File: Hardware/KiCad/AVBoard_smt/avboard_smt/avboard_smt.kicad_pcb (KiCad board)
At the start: 4 copper layers, 177 x 152.1 mm, 119 parts, among them IC1 AS7C256A-10TIN, IC2_AUD0 7432N, IC36 4040N, IC37 7430N, IC39 7400N, IC40 4040N, IC41 7400N, IC43 7400N, IC44 7486N, IC45 7400N, IC46 74257N, IC47 74257N, IC48 74564N, IC4_AUD0 7400N, IC53 7404N, IC6_AUD0 7474N, IC7_AUD0 LM358N, IC9 AS7C256A-10TIN, J1 5V, J2 VID_TO_MOBO, U1 W65C02SP, U2 THS7374, U3 74AHC373, U4 74AHC373, U5 74AHC373, U6 74AC00, U7 74VHC74, U8 74HC244, U9 74HC244

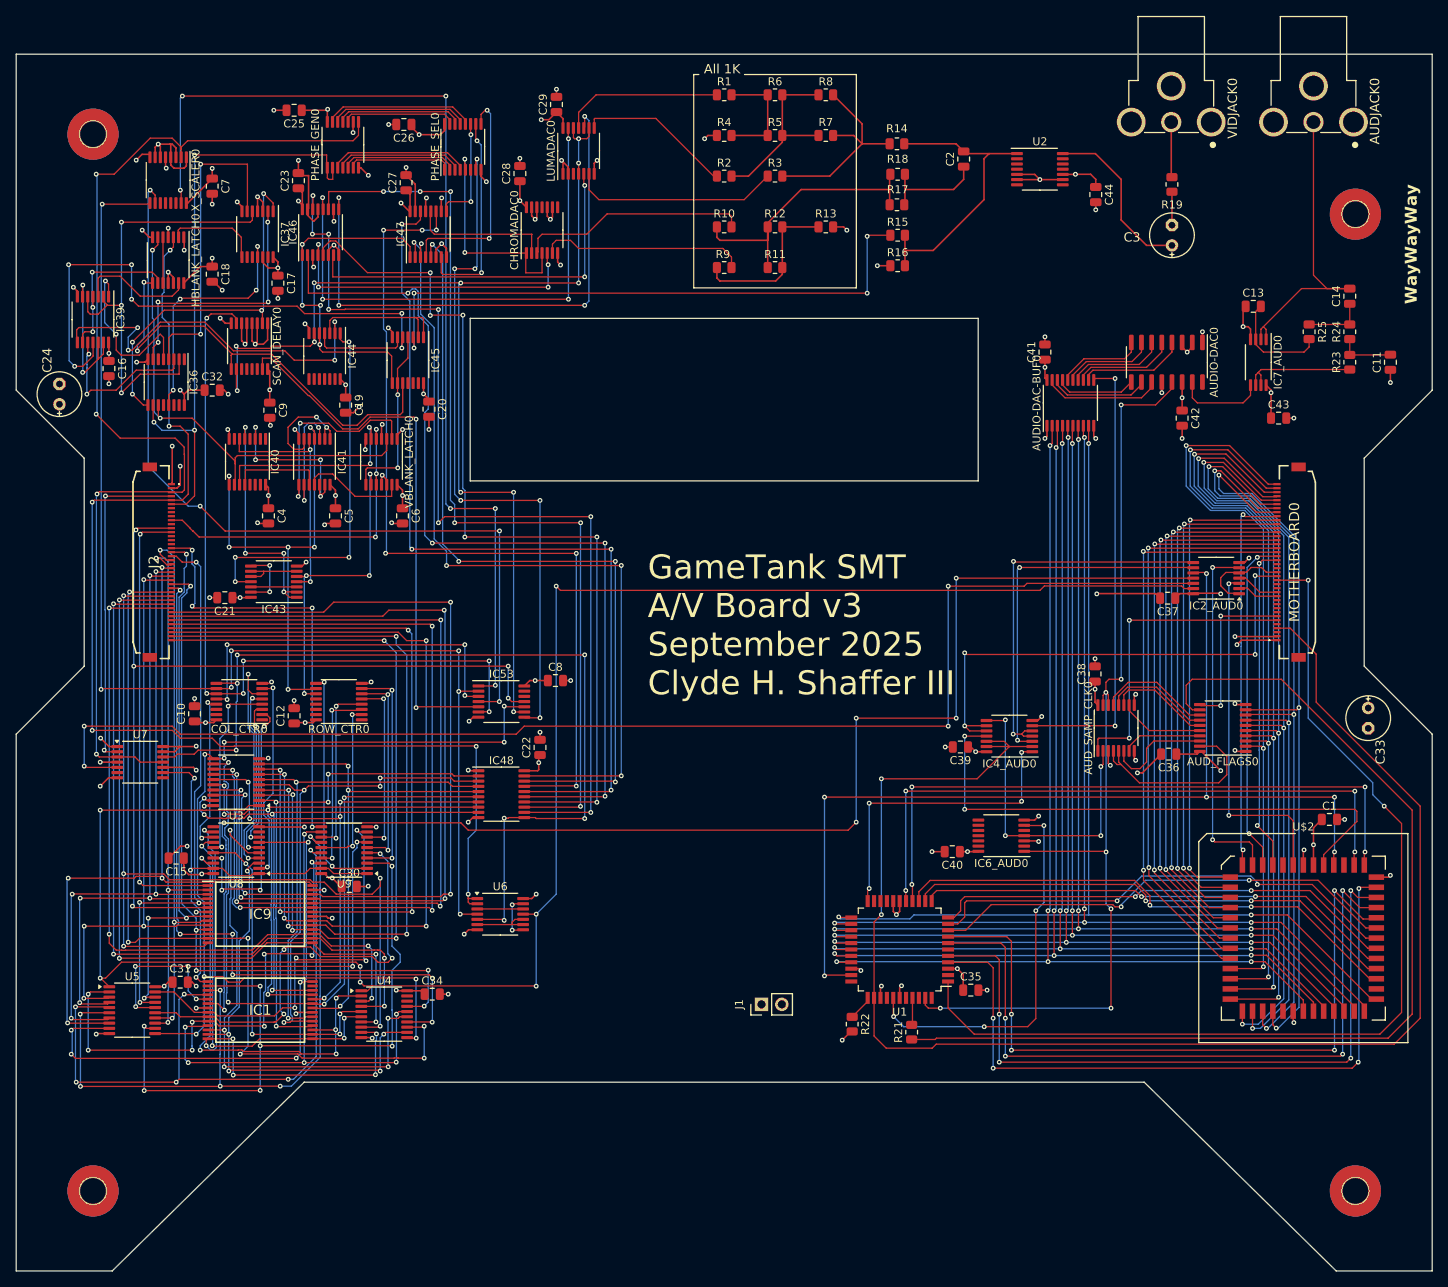
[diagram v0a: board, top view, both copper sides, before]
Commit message: design out the 4K dualport ram
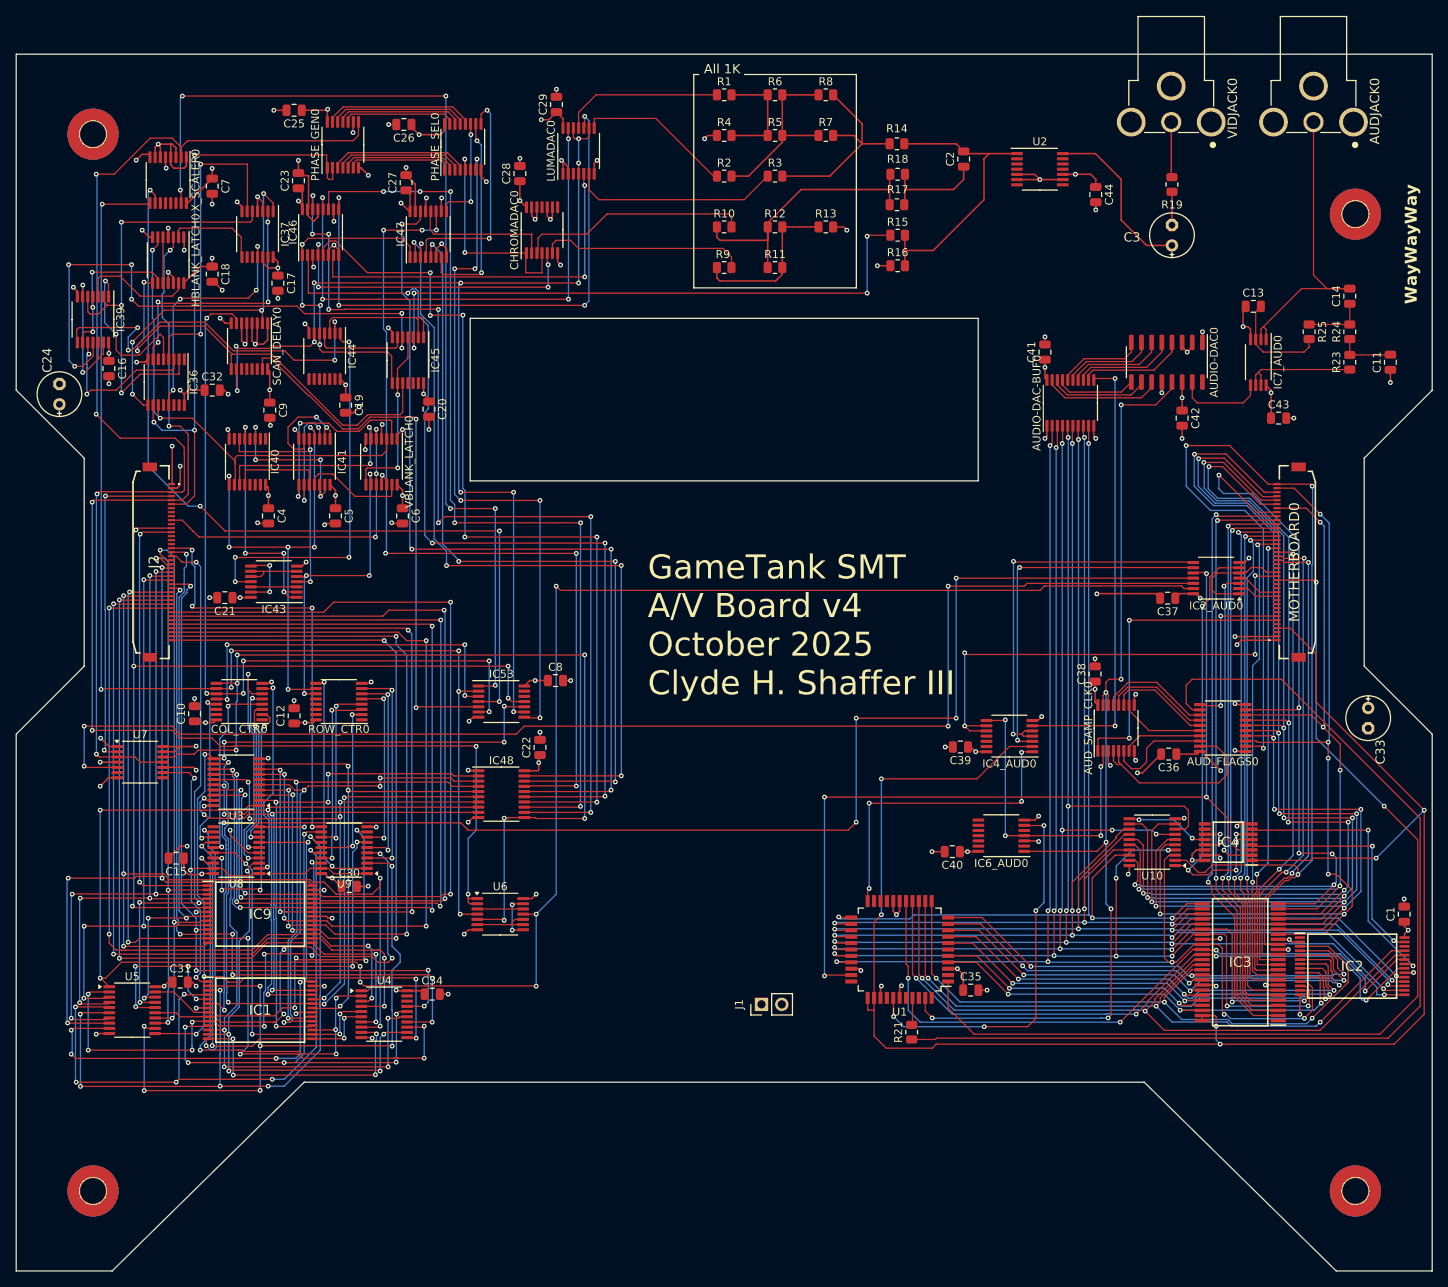
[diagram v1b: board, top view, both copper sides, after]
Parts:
- removed R22: 3.3k, Resistor_SMD:R_0805_2012Metric
- removed U$2: PDPRAM_4KPLCC52S, Package_LCC:PLCC-52_SMD-Socket
- added IC2: IS61C64AL-10TLI, SamacSys_Parts:SOP55P1340X120-28N, F.Cu at (227.0, 155.5)
- added IC3: SN74CBT16210CDLR, SamacSys_Parts:SOP64P1035X279-48N, F.Cu at (213.0, 155.0)
- added IC4: 74VHC157FT, SamacSys_Parts:SOP65P640X120-16N, F.Cu at (211.5, 140.0)
- added U10: 74AHC373, Package_SO:TSSOP-20_4.4x6.5mm_P0.65mm, F.Cu at (202.0, 140.0)
- moved C1 15.1 mm to (233.5, 149.0), turned to 90 degrees
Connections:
- IC2_AUD0 pad 3: Net-(IC2_AUD0A-O) -> /signals_4/Sys_ARAM_~{WE}
- IC2_AUD0 pad 6: Net-(IC2_AUD0B-O) -> /signals_4/Sys_ARAM_~{OE}
- IC4_AUD0 pad 11: Net-(IC4_AUD0D-O) -> unconnected-(IC4_AUD0D-O-Pad11)
- IC4_AUD0 pad 12: /signals_4/CLK14_AUD -> unconnected-(IC4_AUD0D-I0-Pad12)
- IC4_AUD0 pad 13: /signals_4/CLK14_AUD -> unconnected-(IC4_AUD0D-I1-Pad13)
- U1 pad 36: Net-(U1-BE) -> /signals_4/CLK14_AUD
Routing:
- net Net-(IC4_AUD0D-O): track 69.4 -> 0.00 mm, vias 2 -> 0
- net /signals_4/Sys_ARAM_~{OE}: track 0.00 -> 55.8 mm, vias 0 -> 4
- net Net-(AUD_FLAGS0A-1D): track 91.6 -> 143.9 mm, vias 3 -> 4
- net Net-(IC2_AUD0B-O): track 44.6 -> 0.00 mm, vias 2 -> 0
- net Net-(IC2_AUD0A-O): track 44.2 -> 0.00 mm, vias 2 -> 0
- net Net-(AUD_FLAGS0A-3D): track 94.6 -> 133.8 mm, vias 3 -> 6
- net /signals_4/Sys_ARAM_~{WE}: track 0.00 -> 38.9 mm, vias 0 -> 2
- net Net-(AUD_FLAGS0A-4D): track 96.0 -> 134.0 mm, vias 3 -> 6
- net /signals_4/ARAM_~{OE}: track 0.00 -> 35.1 mm, vias 0 -> 2
- net Net-(AUD_FLAGS0A-5D): track 97.7 -> 131.0 mm, vias 3 -> 6
- net /signals_4/AD3: track 132.6 -> 165.2 mm, vias 5 -> 7
- net /signals_4/AA0: track 88.4 -> 58.0 mm, vias 4 -> 3
- net /signals_4/ARAM_~{WE}: track 0.00 -> 29.5 mm, vias 0 -> 2
- net /signals_4/AA2: track 88.8 -> 59.9 mm, vias 4 -> 3
- net Net-(AUD_FLAGS0A-6D): track 97.4 -> 126.2 mm, vias 3 -> 6
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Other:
- board text added: "GameTank SMT A/V Board v4 October 2025 Clyde H. Shaffer III"
- board text removed: "GameTank SMT A/V Board v3 September 2025 Clyde H. Shaffer III"

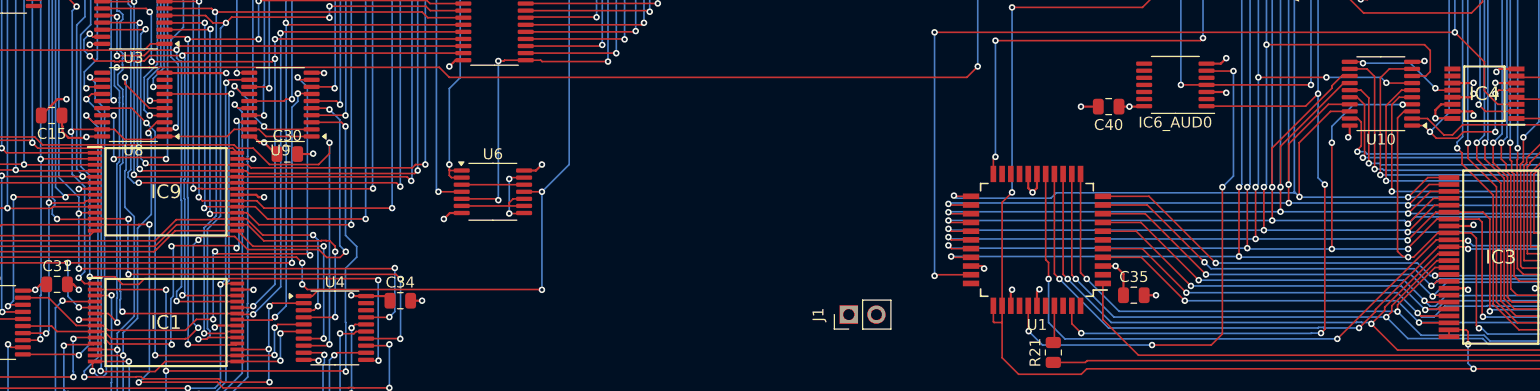
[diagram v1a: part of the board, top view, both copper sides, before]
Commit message: connect loose unused inputs to ground
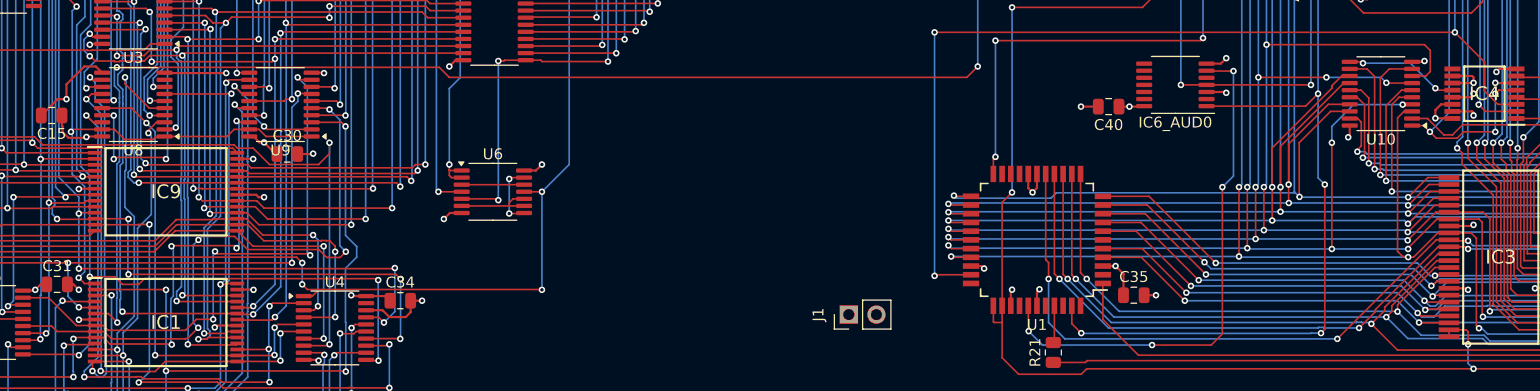
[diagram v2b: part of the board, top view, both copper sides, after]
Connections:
- IC4 pad 10: /signals_4/ACP_ARAM_~{CE} -> GND
- IC4 pad 9: /signals_4/ARAM_~{CE} -> unconnected-(IC4-3Y-Pad9)
- U4 pad 18: unconnected-(U4-D7-Pad18) -> GND
- U8 pad 11: unconnected-(U8-2A3-Pad11) -> GND
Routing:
- net GND: track 234.5 -> 248.1 mm

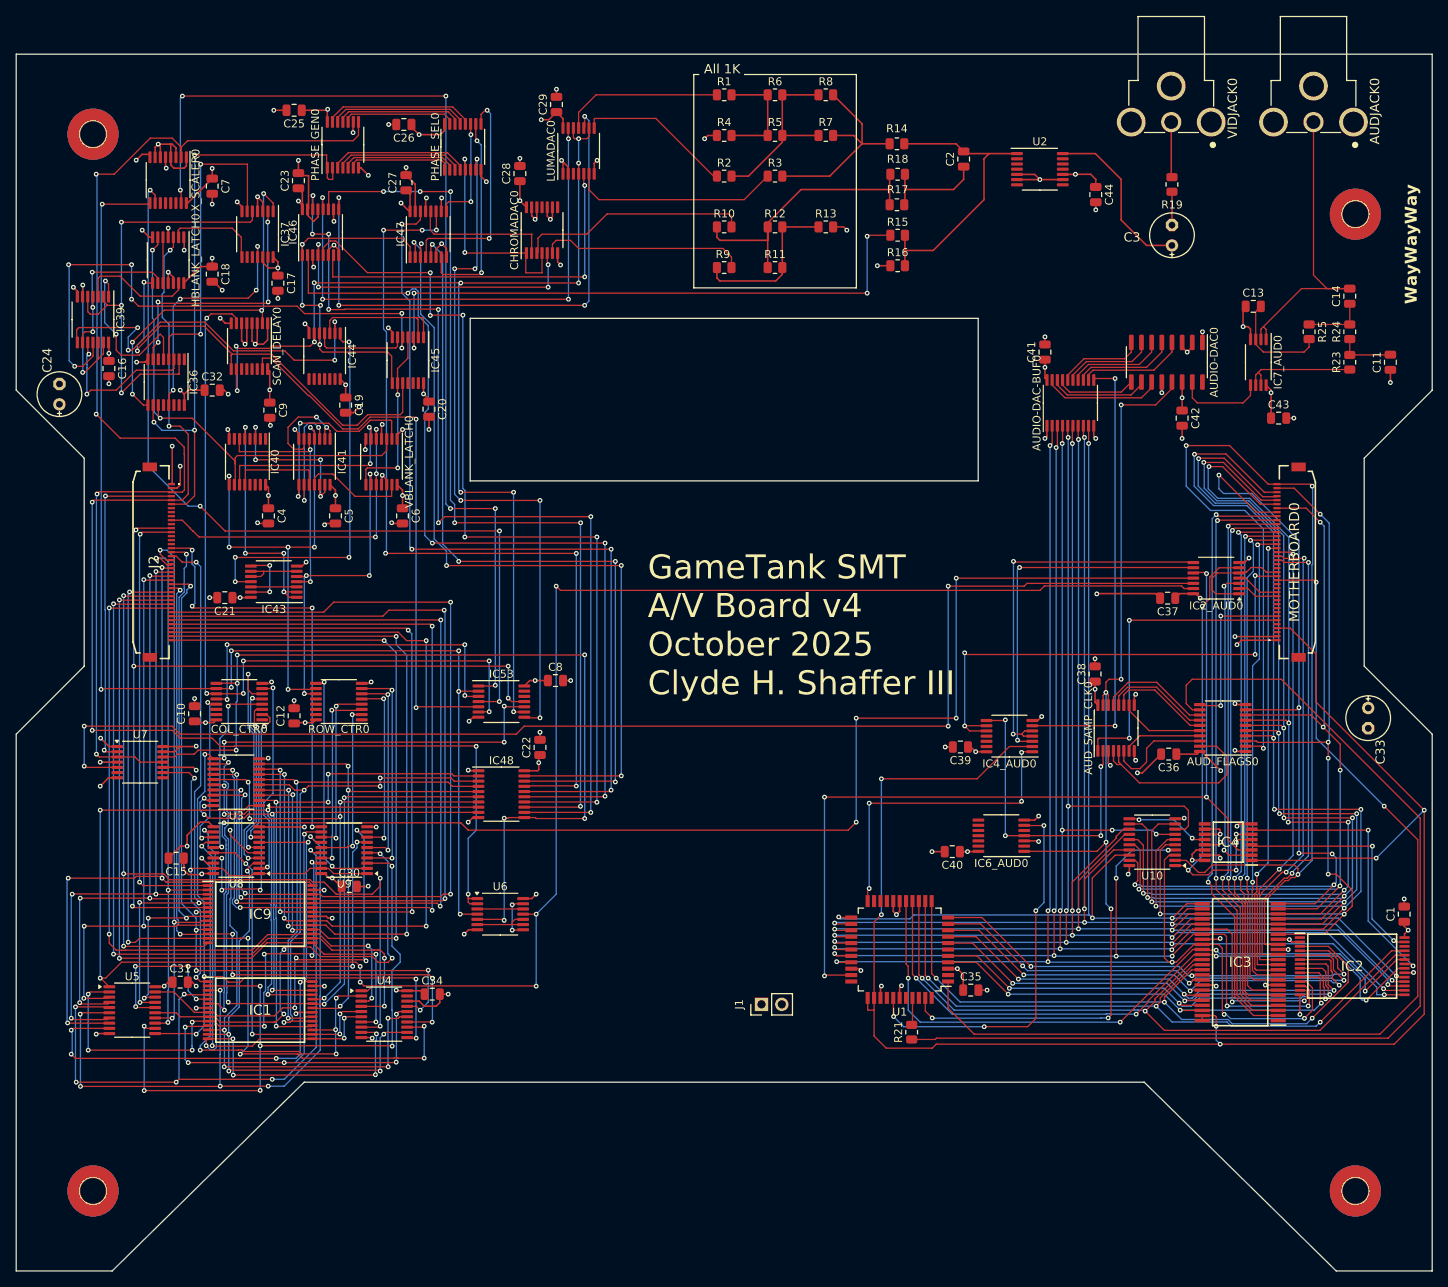
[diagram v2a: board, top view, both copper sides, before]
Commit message: fix composite video generator board
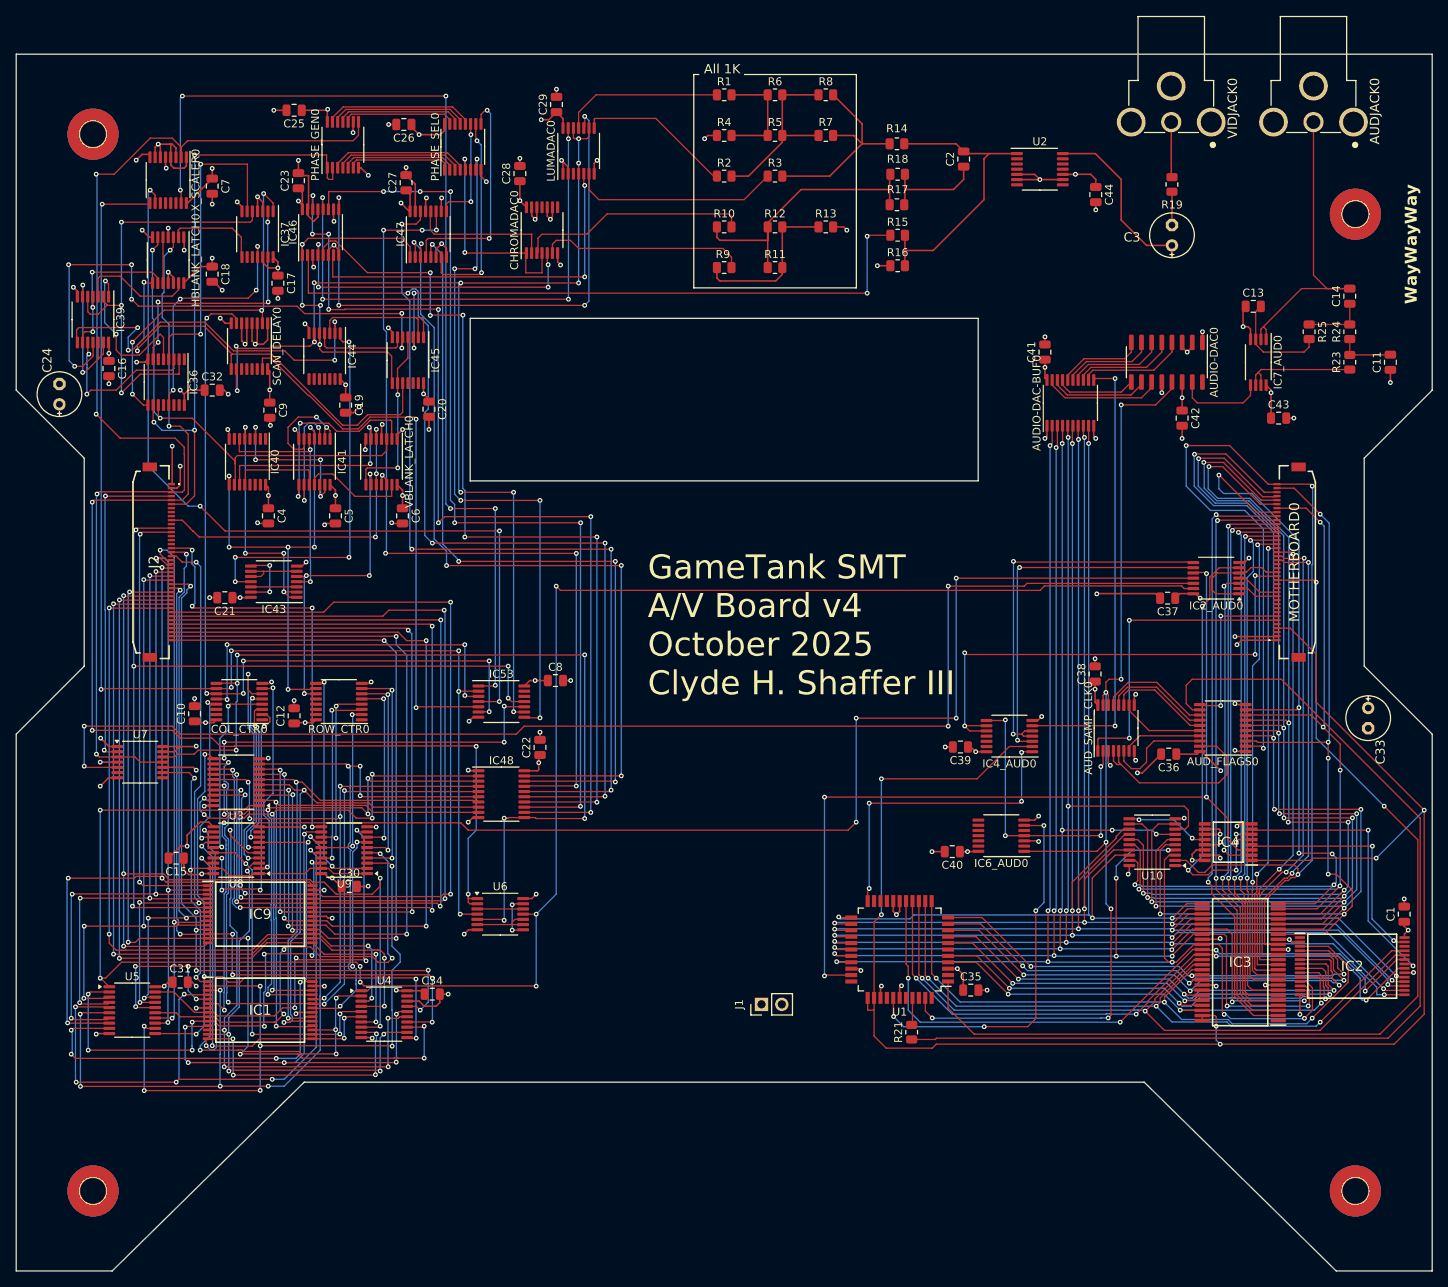
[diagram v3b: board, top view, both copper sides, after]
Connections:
- IC1 pad 18: P7 -> P0
- IC1 pad 19: P6 -> P1
- IC1 pad 20: P5 -> P2
- IC1 pad 22: P4 -> P3
- IC1 pad 23: P3 -> P4
- IC1 pad 24: P2 -> P5
- IC1 pad 25: P1 -> P6
- IC1 pad 26: P0 -> P7
- U3 pad 12: P3 -> P4
- U3 pad 15: P2 -> P5
- U3 pad 16: P1 -> P6
- U3 pad 19: P0 -> P7
- U3 pad 2: P7 -> P0
- U3 pad 5: P6 -> P1
- U3 pad 6: P5 -> P2
- U3 pad 9: P4 -> P3
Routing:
- net P4: track 61.6 -> 89.9 mm, vias 3 -> 4
- net P3: track 89.1 -> 67.5 mm
- net P7: track 63.9 -> 72.0 mm, vias 4 -> 6
- net P6: track 63.5 -> 71.3 mm, vias 4 -> 6
- net P5: track 60.9 -> 66.7 mm, vias 2 -> 5
- net P0: track 65.9 -> 60.8 mm, vias 4 -> 2
- net P1: track 66.4 -> 62.9 mm, vias 4 -> 2
- net P2: track 64.7 -> 61.7 mm, vias 5 -> 2
- net VCC: track 219.1 -> 218.3 mm
- net /Composite Video Generator/HBLANK: track 20.4 -> 19.8 mm
- net MA9: track 87.1 -> 86.5 mm
- net Net-(HBLANK_LATCH0A-D): track 11.9 -> 11.3 mm
- net /Composite Video Generator/XRESET: track 98.9 -> 98.3 mm
- net PAX4: track 33.3 -> 32.7 mm
- net /signals_4/AD5: track 156.7 -> 156.2 mm
